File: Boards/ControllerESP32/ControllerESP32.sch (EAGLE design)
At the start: 14 parts

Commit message: cleaned up some stuff
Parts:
- removed BLE1: BLUEFRUITLE-SPI, Library:BLUEFRUITLE-SPI
- removed DS2: (no value), SparkFun-Connectors:CONN_03LONGPADS
- removed SR1: SN74HC595N, SparkFun-IC-Logic:74HC595N
- removed ST2: (no value), SparkFun-Connectors:CONN_04LONGPADS
- removed STC2: POLOLU-MD09B, Library:POLOLU-MD09B
- added U$1: ESP32-DEV, IAD-Library:ESP32-DEV
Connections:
- net ST1_BLUE renamed ST_BLUE
- net ST1_GREEN renamed ST_GREEN
- net ST1_RED renamed ST_RED
- net ST1_YELLOW renamed ST_YELLOW
- removed net BLE_CS: BLE1.CS, MCU1.D7(INT)
- removed net BLE_IRQ: BLE1.IRQ, MCU1.D6(INT)
- removed net BLE_MISO: BLE1.MISO, MCU1.D10(MISO)
- removed net BLE_MOSI: BLE1.MOSI, MCU1.D8(INT,MOSI)
- removed net BLE_SCK: BLE1.SCK, MCU1.D9(SCK)
- removed net DS2_SIG: DS2.3, MCU1.A1(INT)
- removed net N$6: STC2.RST, STC2.SLP
- removed net SR1_RCK: MCU1.D0(INT), SR1.RCK
- removed net SR1_SCK: MCU1.D1(INT), SR1.SCK
- removed net SR1_SER: MCU1.A6, MCU1.D12(SCL), SR1.SER
- removed net ST2_BLUE: ST2.1, STC2.1B
- removed net ST2_GREEN: ST2.4, STC2.2B
- removed net ST2_RED: ST2.3, STC2.2A
- removed net ST2_YELLOW: ST2.2, STC2.1A
- removed net STC1_DIR: MCU1.D5(INT), STC1.DIR
- removed net STC1_EN: SR1.QH, STC1.EN
- removed net STC1_MS1: SR1.QG, STC1.MS1
- removed net STC1_MS2: SR1.QF, STC1.MS2
- removed net STC1_MS3: SR1.QE, STC1.MS3
- removed net STC1_STEP: MCU1.D4(INT), STC1.STEP
- removed net STC2_DIR: MCU1.D2, STC2.DIR
- removed net STC2_EN: SR1.QD, STC2.EN
- removed net STC2_MS1: SR1.QC, STC2.MS1
- removed net STC2_MS2: SR1.QB, STC2.MS2
- removed net STC2_MS3: SR1.QA, STC2.MS3
- removed net STC2_STEP: MCU1.D3, STC2.STEP
- new net STC_DIR: MCU1.D0(INT), STC1.DIR
- new net STC_EN: MCU1.D5(INT), STC1.EN
- new net STC_MS1: MCU1.D4(INT), STC1.MS1
- new net STC_MS2: MCU1.D3, STC1.MS2
- new net STC_MS3: MCU1.D2, STC1.MS3
- new net STC_STEP: MCU1.D1(INT), STC1.STEP
- net 12V: no longer STC2.VMOT
- net 3V: now also DS1.3; no longer BLE1.VIN, DS1.1, DS2.1, SR1.SCL, SR1.VCC, STC2.VDD
- net DS1_SIG: now also DS1.2; no longer DS1.3
- net GND: now also DS1.1; no longer BLE1.GND, DS1.2, DS2.2, SR1.G, SR1.GND, STC2.GMOT, STC2.GND
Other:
- moved on the sheet: DS1, ST1

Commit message: finished esp32 based board
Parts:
- removed MCU1: MKR1000, Library:MKR1000
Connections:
- net 3V: now also U$1.3V3; no longer MCU1.VCC
- net 5V: now also U$1.5V; no longer MCU1.VIN
- net DS1_SIG: now also U$1.IO13; no longer MCU1.A0/DAC0
- net GND: now also U$1.GND1, U$1.GND2, U$1.GND3; no longer MCU1.GND
- net STC_DIR: now also U$1.IO33; no longer MCU1.D0(INT)
- net STC_EN: now also U$1.IO12; no longer MCU1.D5(INT)
- net STC_MS1: now also U$1.IO14; no longer MCU1.D4(INT)
- net STC_MS2: now also U$1.IO27; no longer MCU1.D3
- net STC_MS3: now also U$1.IO26; no longer MCU1.D2
- net STC_STEP: now also U$1.IO25; no longer MCU1.D1(INT)
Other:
- moved on the sheet: U$1
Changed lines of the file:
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@@
 </classes>
 <parts>
-<part name="MCU1" library="Library" deviceset="MKR1000" device=""/>
 <part name="STC1" library="Library" deviceset="POLOLU-MD09B" device=""/>
 <part name="PW1" library="SparkFun-Connectors" deviceset="CONN_02" device="5MM"/>
@@
 </plain>
 <instances>
-<instance part="MCU1" gate="G$1" x="30.48" y="60.96"/>
 <instance part="STC1" gate="G$1" x="48.26" y="12.7"/>
 <instance part="PW1" gate="G$1" x="157.48" y="45.72"/>
@@
 <instance part="C3" gate="G$1" x="106.68" y="33.02" rot="R90"/>
 <instance part="DS1" gate="J$1" x="99.06" y="73.66"/>
-<instance part="U$1" gate="G$1" x="-43.18" y="60.96"/>
+<instance part="U$1" gate="G$1" x="43.18" y="78.74"/>
 </instances>
 <busses>
@@
 <nets>
 <net name="GND" class="0">
-<segment>
-<pinref part="MCU1" gate="G$1" pin="GND"/>
-<wire x1="50.8" y1="71.12" x2="71.12" y2="71.12" width="0.1524" layer="91"/>
-<label x="58.42" y="71.12" size="1.778" layer="95"/>
-</segment>
 <segment>
 <pinref part="STC1" gate="G$1" pin="GND"/>
@@
 <label x="114.3" y="71.12" size="1.778" layer="95"/>
 </segment>
+<segment>
+<pinref part="U$1" gate="G$1" pin="GND3"/>
+<wire x1="60.96" y1="101.6" x2="76.2" y2="101.6" width="0.1524" layer="91"/>
+<label x="68.58" y="101.6" size="1.778" layer="95"/>
+</segment>
+<segment>
+<pinref part="U$1" gate="G$1" pin="GND2"/>
+<wire x1="60.96" y1="86.36" x2="76.2" y2="86.36" width="0.1524" layer="91"/>
+<label x="68.58" y="86.36" size="1.778" layer="95"/>
+</segment>
+<segment>
+<pinref part="U$1" gate="G$1" pin="GND1"/>
+<wire x1="27.94" y1="68.58" x2="10.16" y2="68.58" width="0.1524" layer="91"/>
+<label x="10.16" y="68.58" size="1.778" layer="95"/>
+</segment>
 </net>
 <net name="3V" class="0">
-<segment>
-<pinref part="MCU1" gate="G$1" pin="VCC"/>
-<wire x1="50.8" y1="73.66" x2="71.12" y2="73.66" width="0.1524" layer="91"/>
-<label x="58.42" y="73.66" size="1.778" layer="95"/>
-</segment>
 <segment>
 <pinref part="STC1" gate="G$1" pin="VDD"/>
@@
 <wire x1="106.68" y1="76.2" x2="129.54" y2="76.2" width="0.1524" layer="91"/>
 <label x="114.3" y="76.2" size="1.778" layer="95"/>
+</segment>
+<segment>
+<pinref part="U$1" gate="G$1" pin="3V3"/>
+<wire x1="27.94" y1="101.6" x2="10.16" y2="101.6" width="0.1524" layer="91"/>
+<label x="10.16" y="101.6" size="1.778" layer="95"/>
 </segment>
 </net>
@@
 </segment>
 <segment>
-<pinref part="MCU1" gate="G$1" pin="D5(INT)"/>
-<wire x1="10.16" y1="45.72" x2="-7.62" y2="45.72" width="0.1524" layer="91"/>
-<label x="-7.62" y="45.72" size="1.778" layer="95"/>
+<pinref part="U$1" gate="G$1" pin="IO12"/>
+<wire x1="27.94" y1="71.12" x2="10.16" y2="71.12" width="0.1524" layer="91"/>
+<label x="10.16" y="71.12" size="1.778" layer="95"/>
 </segment>
 </net>
@@
 </segment>
 <segment>
-<pinref part="MCU1" gate="G$1" pin="D0(INT)"/>
-<wire x1="10.16" y1="58.42" x2="-7.62" y2="58.42" width="0.1524" layer="91"/>
-<label x="-7.62" y="58.42" size="1.778" layer="95"/>
+<pinref part="U$1" gate="G$1" pin="IO33"/>
+<wire x1="27.94" y1="83.82" x2="10.16" y2="83.82" width="0.1524" layer="91"/>
+<label x="10.16" y="83.82" size="1.778" layer="95"/>
 </segment>
 </net>
@@
 </segment>
 <segment>
-<pinref part="MCU1" gate="G$1" pin="D1(INT)"/>
-<wire x1="10.16" y1="55.88" x2="-7.62" y2="55.88" width="0.1524" layer="91"/>
-<label x="-7.62" y="55.88" size="1.778" layer="95"/>
+<pinref part="U$1" gate="G$1" pin="IO25"/>
+<wire x1="27.94" y1="81.28" x2="10.16" y2="81.28" width="0.1524" layer="91"/>
+<label x="10.16" y="81.28" size="1.778" layer="95"/>
 </segment>
 </net>
@@
 </segment>
 <segment>
-<pinref part="MCU1" gate="G$1" pin="D2"/>
-<wire x1="10.16" y1="53.34" x2="-7.62" y2="53.34" width="0.1524" layer="91"/>
-<label x="-7.62" y="53.34" size="1.778" layer="95"/>
+<pinref part="U$1" gate="G$1" pin="IO26"/>
+<wire x1="27.94" y1="78.74" x2="10.16" y2="78.74" width="0.1524" layer="91"/>
+<label x="10.16" y="78.74" size="1.778" layer="95"/>
 </segment>
 </net>
@@
 </segment>
 <segment>
-<pinref part="MCU1" gate="G$1" pin="D4(INT)"/>
-<wire x1="10.16" y1="48.26" x2="-7.62" y2="48.26" width="0.1524" layer="91"/>
-<label x="-7.62" y="48.26" size="1.778" layer="95"/>
+<pinref part="U$1" gate="G$1" pin="IO14"/>
+<wire x1="27.94" y1="73.66" x2="10.16" y2="73.66" width="0.1524" layer="91"/>
+<label x="10.16" y="73.66" size="1.778" layer="95"/>
 </segment>
 </net>
@@
 </segment>
 <segment>
-<pinref part="MCU1" gate="G$1" pin="D3"/>
-<wire x1="10.16" y1="50.8" x2="-7.62" y2="50.8" width="0.1524" layer="91"/>
-<label x="-7.62" y="50.8" size="1.778" layer="95"/>
+<pinref part="U$1" gate="G$1" pin="IO27"/>
+<wire x1="27.94" y1="76.2" x2="10.16" y2="76.2" width="0.1524" layer="91"/>
+<label x="10.16" y="76.2" size="1.778" layer="95"/>
 </segment>
 </net>
@@
 </segment>
 <segment>
-<pinref part="MCU1" gate="G$1" pin="VIN"/>
-<wire x1="50.8" y1="76.2" x2="71.12" y2="76.2" width="0.1524" layer="91"/>
-<label x="58.42" y="76.2" size="1.778" layer="95"/>
+<pinref part="U$1" gate="G$1" pin="5V"/>
+<wire x1="27.94" y1="55.88" x2="10.16" y2="55.88" width="0.1524" layer="91"/>
+<label x="10.16" y="55.88" size="1.778" layer="95"/>
 </segment>
 </net>
@@
 </segment>
 <segment>
-<pinref part="MCU1" gate="G$1" pin="A0/DAC0"/>
-<wire x1="10.16" y1="76.2" x2="-7.62" y2="76.2" width="0.1524" layer="91"/>
-<label x="-7.62" y="76.2" size="1.778" layer="95"/>
-</segment>
-</net>
+<pinref part="U$1" gate="G$1" pin="IO13"/>
+<wire x1="27.94" y1="66.04" x2="10.16" y2="66.04" width="0.1524" layer="91"/>
+<label x="10.16" y="66.04" size="1.778" layer="95"/>
+</segment>
+</net>

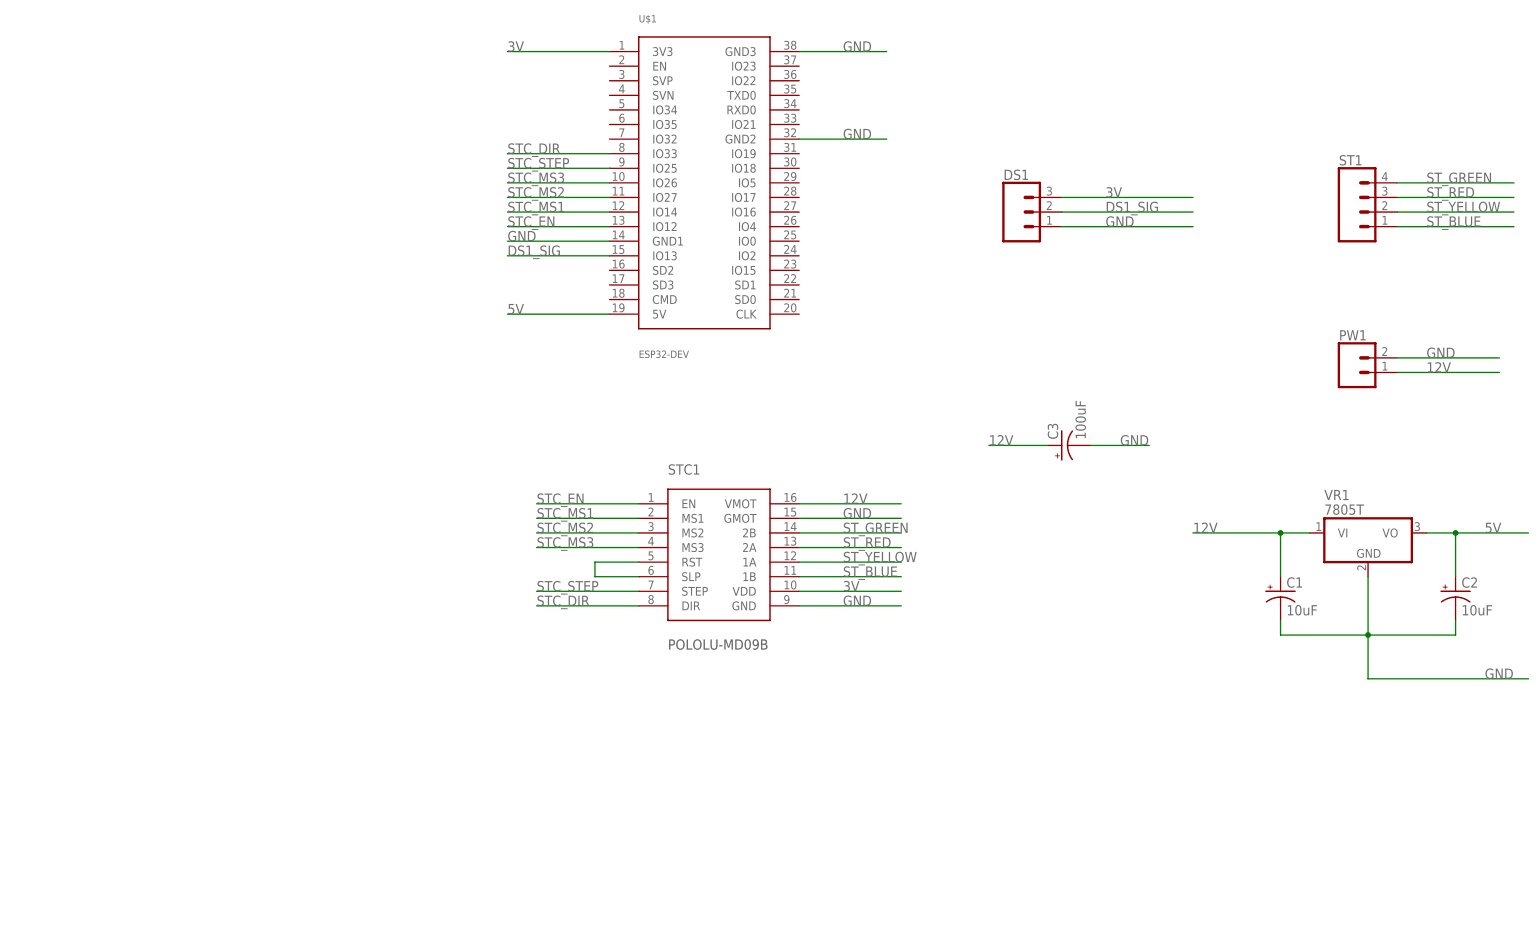
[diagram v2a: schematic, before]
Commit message: finish esp32 based controller
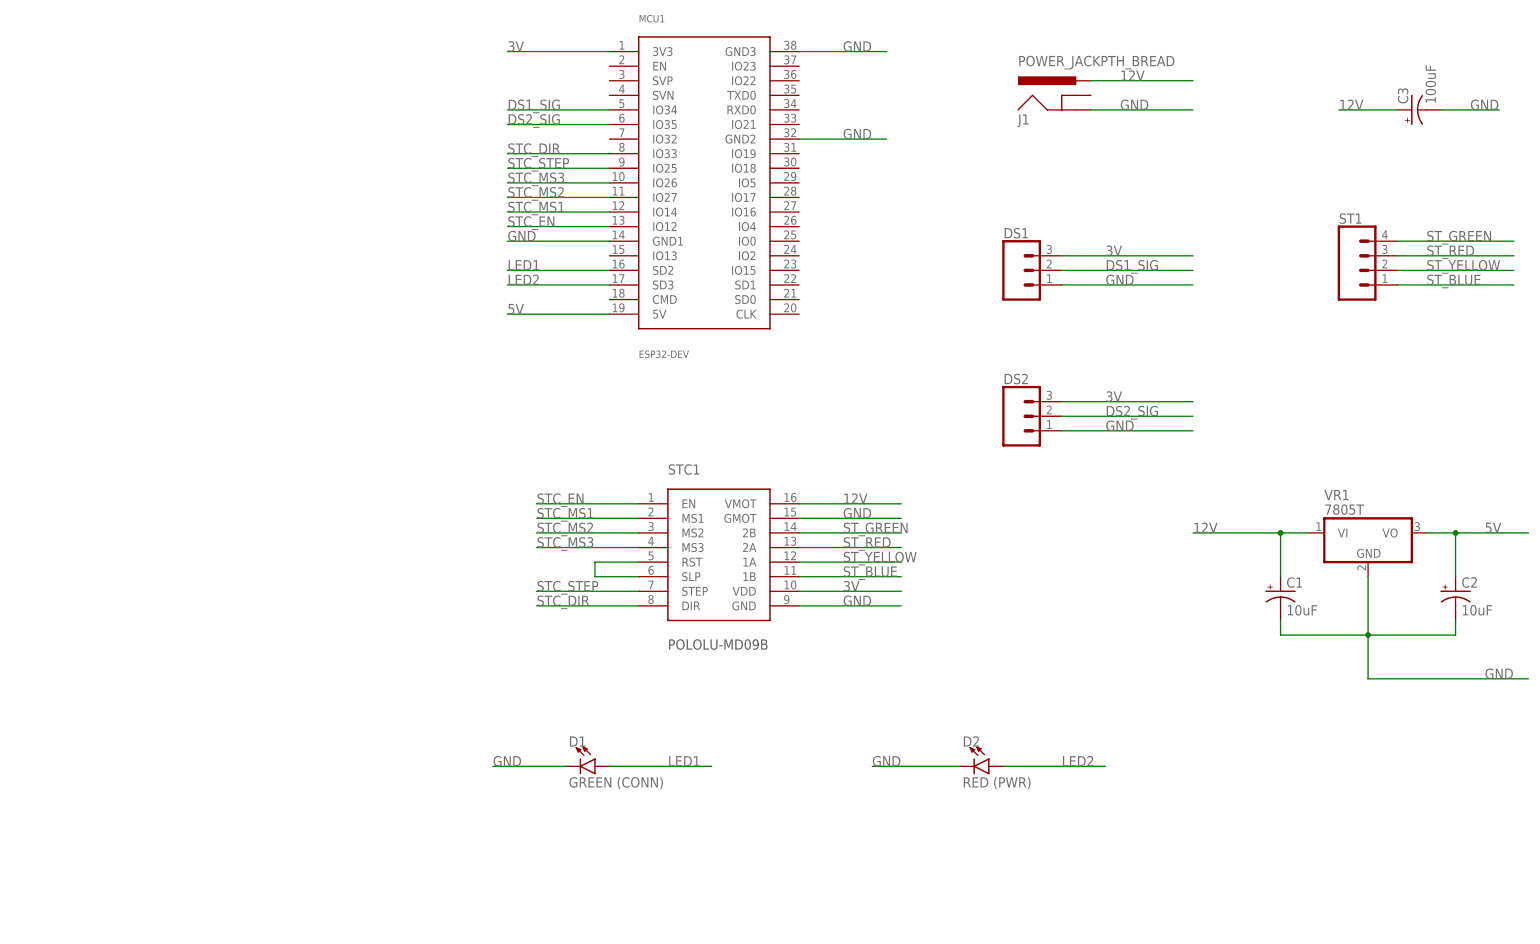
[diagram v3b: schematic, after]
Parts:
- removed PW1: (no value), SparkFun-Connectors:CONN_025MM
- added D1: GREEN (CONN), SparkFun-LED:LED5MM
- added D2: RED (PWR), SparkFun-LED:LED5MM
- added DS2: (no value), SparkFun-Connectors:CONN_03LONGPADS
- added J1: POWER_JACKPTH_BREAD, SparkFun-Connectors:POWER_JACKPTH_BREAD
- renumbered U$1 to MCU1
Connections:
- new net DS2_SIG: DS2.2, MCU1.IO35
- new net LED1: D1.A, MCU1.SD2
- new net LED2: D2.A, MCU1.SD3
- net 12V: now also J1.PWR; no longer PW1.1
- net 3V: now also DS2.3
- net DS1_SIG: now also MCU1.IO34; no longer MCU1.IO13
- net GND: now also D1.C, D2.C, DS2.1, J1.GND; no longer PW1.2
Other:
- moved on the sheet: C3, DS1, ST1

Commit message: finished esp32 board based board
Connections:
- net LED1: now also MCU1.IO19; no longer MCU1.SD2
- net LED2: now also MCU1.IO18; no longer MCU1.SD3
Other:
- note added: "Use IO19 and IO18 for LEDs"
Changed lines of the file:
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@@
 <sheet>
 <plain>
+<text x="93.98" y="78.74" size="1.778" layer="94">Use IO19 and IO18 for LEDs</text>
 </plain>
 <instances>
@@
 <net name="LED1" class="0">
 <segment>
-<pinref part="MCU1" gate="G$1" pin="SD2"/>
-<wire x1="27.94" y1="63.5" x2="10.16" y2="63.5" width="0.1524" layer="91"/>
-<label x="10.16" y="63.5" size="1.778" layer="95"/>
-</segment>
-<segment>
 <pinref part="D1" gate="G$1" pin="A"/>
 <wire x1="27.94" y1="-22.86" x2="45.72" y2="-22.86" width="0.1524" layer="91"/>
 <label x="38.1" y="-22.86" size="1.778" layer="95"/>
 </segment>
+<segment>
+<pinref part="MCU1" gate="G$1" pin="IO19"/>
+<wire x1="60.96" y1="83.82" x2="76.2" y2="83.82" width="0.1524" layer="91"/>
+<label x="68.58" y="83.82" size="1.778" layer="95"/>
+</segment>
 </net>
 <net name="LED2" class="0">
-<segment>
-<pinref part="MCU1" gate="G$1" pin="SD3"/>
-<wire x1="27.94" y1="60.96" x2="10.16" y2="60.96" width="0.1524" layer="91"/>
-<label x="10.16" y="60.96" size="1.778" layer="95"/>
-</segment>
 <segment>
 <pinref part="D2" gate="G$1" pin="A"/>
@@
 <label x="106.68" y="-22.86" size="1.778" layer="95"/>
 </segment>
-</net>
+<segment>
+<pinref part="MCU1" gate="G$1" pin="IO18"/>
+<wire x1="60.96" y1="81.28" x2="76.2" y2="81.28" width="0.1524" layer="91"/>
+<label x="68.58" y="81.28" size="1.778" layer="95"/>
+</segment>
+</net>
